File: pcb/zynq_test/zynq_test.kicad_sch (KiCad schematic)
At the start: 0 parts

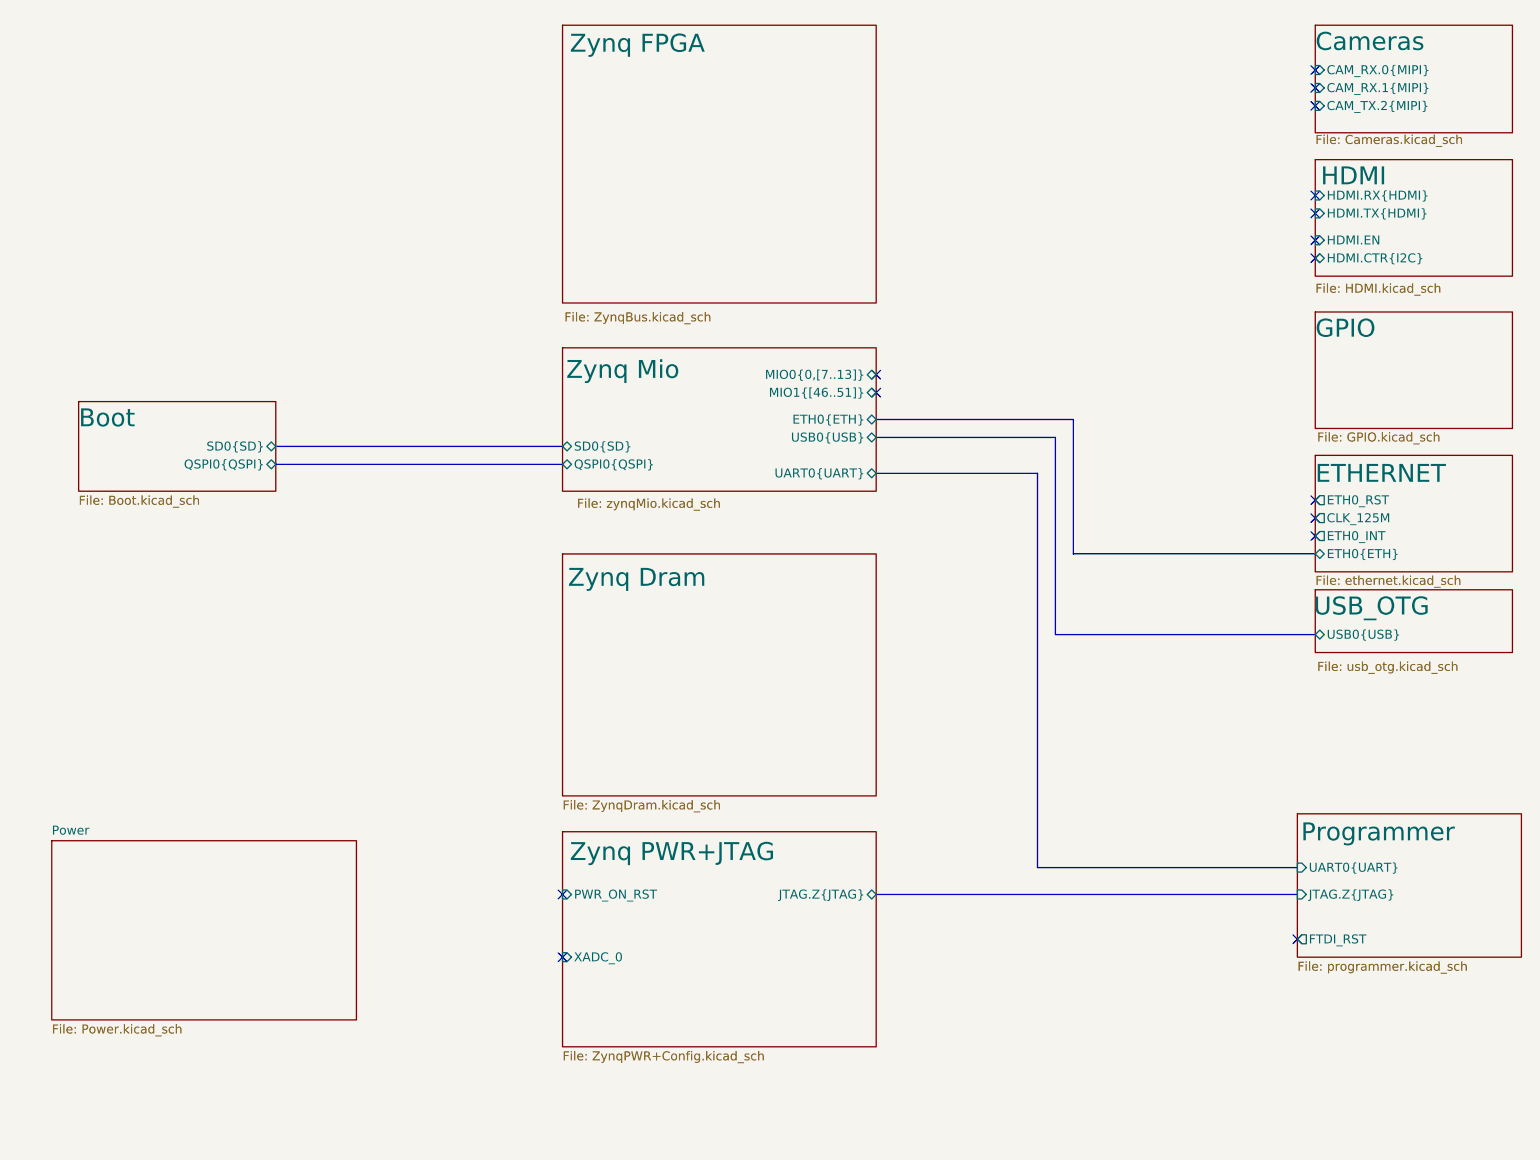
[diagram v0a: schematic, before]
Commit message: Finished most of the schematic, will start routing soon
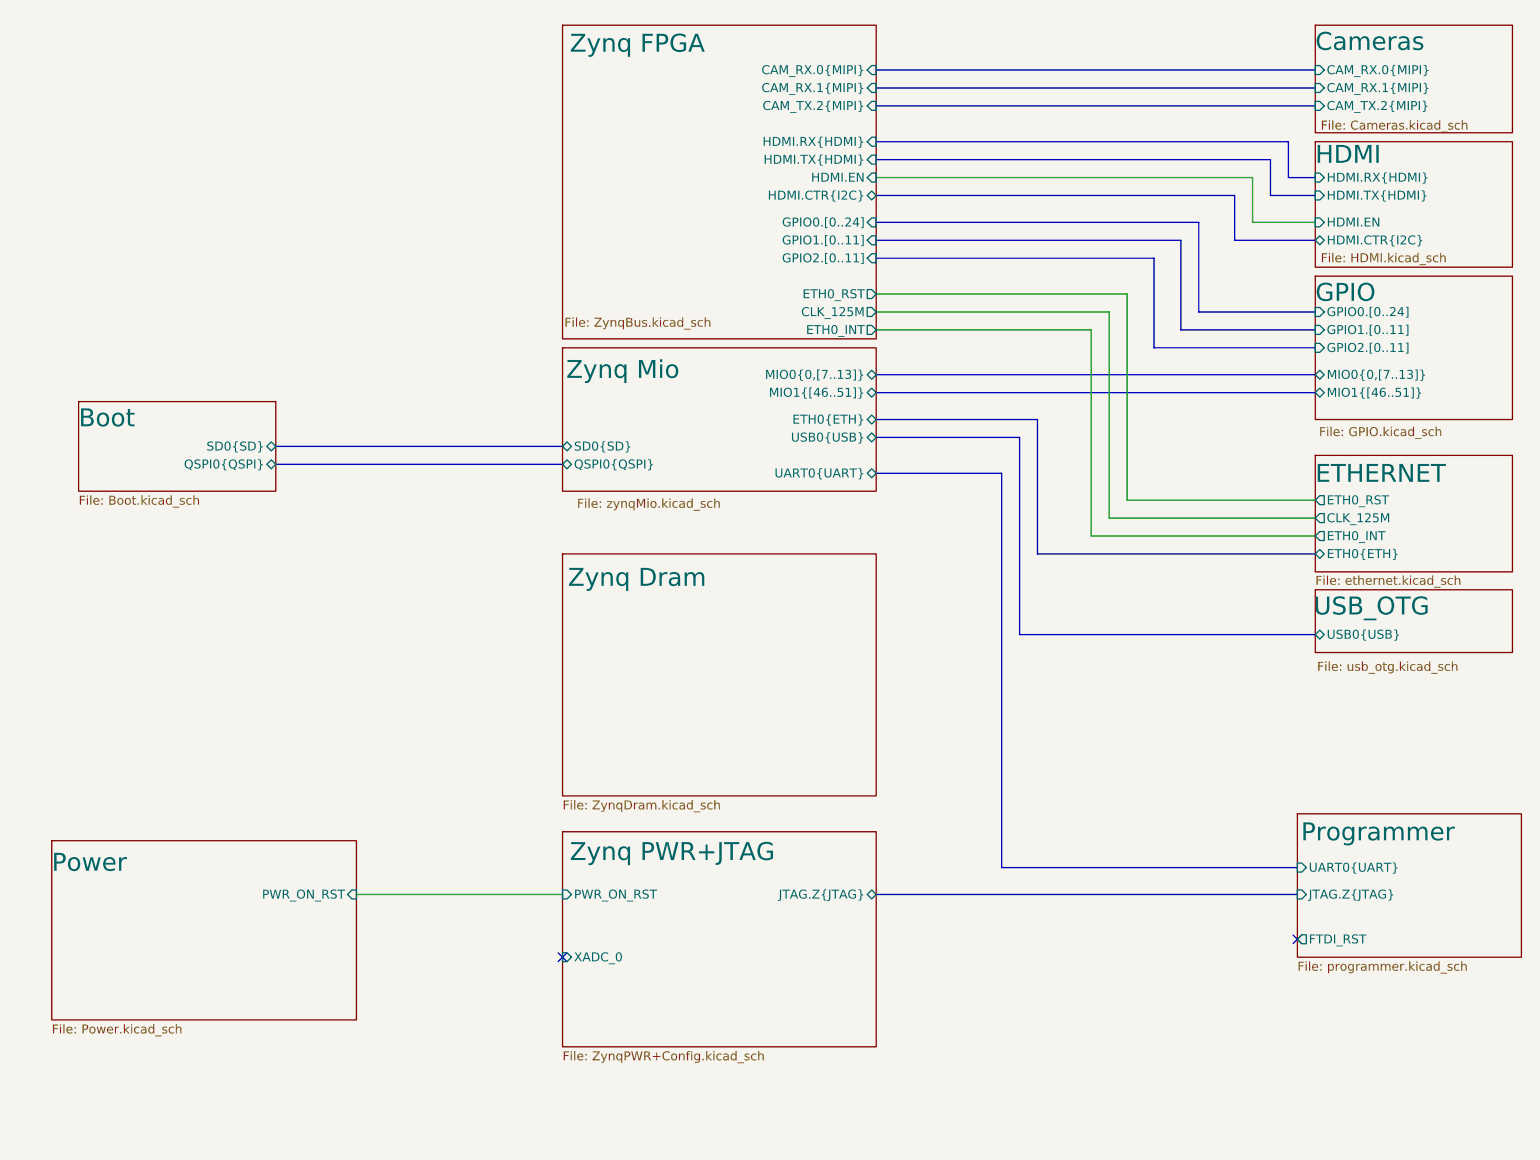
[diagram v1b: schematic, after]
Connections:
- no-connect marks 15 -> 2
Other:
- sheet GPIO ports: added GPIO0.[0..24], GPIO1.[0..11], GPIO2.[0..11], MIO0{0,[7..13]}, MIO1{[46..51]}; removed none
- sheet Power ports: added PWR_ON_RST; removed none
- sheet Zynq FPGA ports: added CAM_RX.0{MIPI}, CAM_RX.1{MIPI}, CAM_TX.2{MIPI}, CLK_125M, ETH0_INT, ETH0_RST, GPIO0.[0..24], GPIO1.[0..11], GPIO2.[0..11], HDMI.CTR{I2C}, HDMI.EN, HDMI.RX{HDMI}, HDMI.TX{HDMI}; removed none

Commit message: Almost done with BOM
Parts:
- added H101, H102, H103, H104: MountingHole_Pad, MountingHole:MountingHole_3.2mm_M3_DIN965_Pad, symbol Mechanical:MountingHole_Pad
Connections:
- new net GND: H101.1, H102.1, H103.1, H104.1
- no-connect marks 2 -> 1
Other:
- sheet Cameras ports: added CAM_CTR{I2C}; removed none
- sheet Programmer ports: added POR_B; removed FTDI_RST
- sheet Zynq FPGA ports: added CAM_CTR{I2C}; removed none
